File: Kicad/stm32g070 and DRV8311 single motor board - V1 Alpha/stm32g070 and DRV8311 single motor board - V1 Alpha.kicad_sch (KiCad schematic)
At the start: 34 parts, among them J1 JST SH SM04B, J2 JST SH SM06B, J4 Conn_01x02_Pin, SW1 SW_Push, U1 STM32G070CBTr, Y1 ABM8-16.000MHZ-10-1-U-T

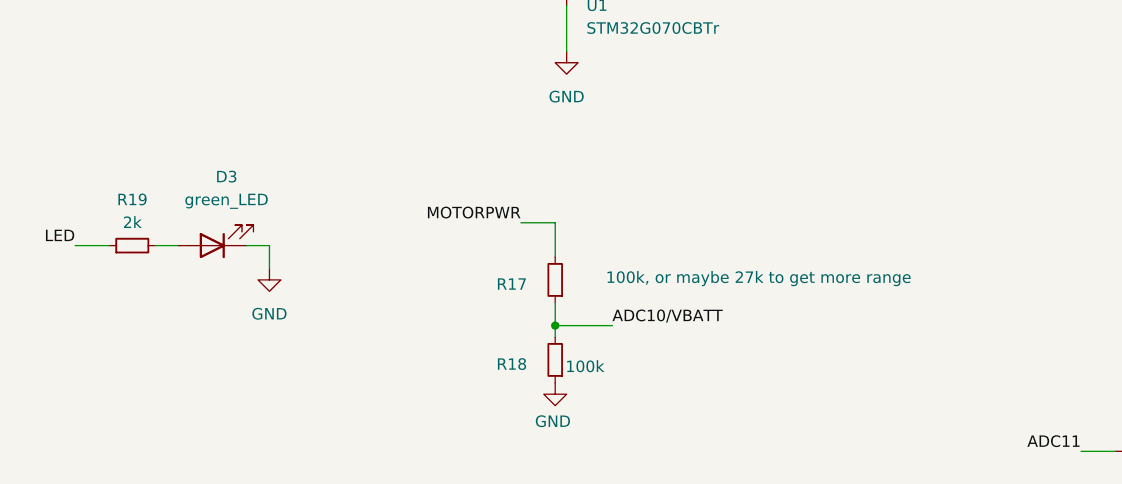
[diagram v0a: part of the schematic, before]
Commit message: Fixes to the PCB after production related to mosfets
So..... I sourced the wrong mosfets. I chose mosfets with the marketing moniker PowerPAK, never thinking that could mean multiple footprint sizes. I sourced mosfets with the powerpak 1212 footprint, instead of the powerpak SO-8 footprint. They ended up being tiny and I had to do a bodge fix to test. I have replaced the mosfets in schematic with correctly sized ones now.

Another change I made in this commit is related to LEDs. I sourced the leds and resistors last minute, so the values are a bit different than originally on the schematic. I realized too that my tri-state led status circuit wouldn't work, because the bq25060 status pin is not a tri-state and I couldn't make it one. I now only have one led to indicate charging. I have updated the schematics and board with the values and single status led.

The big capacitors I sourced differently, I wasn't able to get a small 220uF, so I got a big aluminum polarized 220uF and put it in place of the 1000uF. All the other capacitors are different too, I realized the voltage rating doesn't matter on some, so to cut down BOM part number if there was a capacitor value with two separate voltages, I just went with 16v one.

Gerber files have been updated.
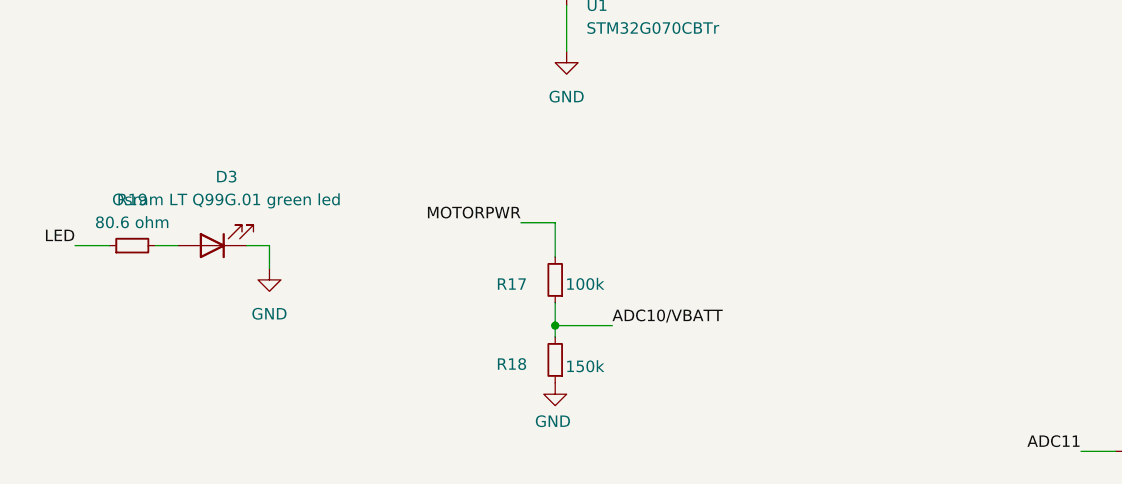
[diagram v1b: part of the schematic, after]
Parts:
- D3: value green_LED -> Osram LT Q99G.01 green led
- R17: value 100k, or maybe 27k to get more range -> 100k
- R18: value 100k -> 150k
- R19: value 2k -> 80.6 ohm
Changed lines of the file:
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@@
 			)
 		)
-		(property "Value" "100k"
+		(property "Value" "150k"
 			(at 78.232 182.372 0)
 			(effects
@@
 			)
 		)
-		(property "Value" "100k, or maybe 27k to get  more range"
-			(at 97.536 172.466 0)
+		(property "Value" "100k"
+			(at 78.232 173.228 0)
 			(effects
 				(font
@@
 			)
 		)
-		(property "Value" "green_LED"
+		(property "Value" "Osram LT Q99G.01 green led"
 			(at 38.4175 163.83 0)
 			(effects
@@
 			)
 		)
-		(property "Value" "2k"
+		(property "Value" "80.6 ohm"
 			(at 27.94 166.37 90)
 			(effects
